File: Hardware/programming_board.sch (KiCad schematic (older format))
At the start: 41 parts, among them J1 Conn_02x03_Odd_Even, J10 Conn_02x03_Odd_Even, J11 Conn_01x05, J12 USB_C_Receptacle_USB2.0, J2 Conn_02x10_Odd_Even, J3 Conn_02x04_Odd_Even, J4 Conn_02x03_Odd_Even, J6 Conn_02x05_Odd_Even, J7 Conn_02x05_Odd_Even, J8 Conn_01x05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

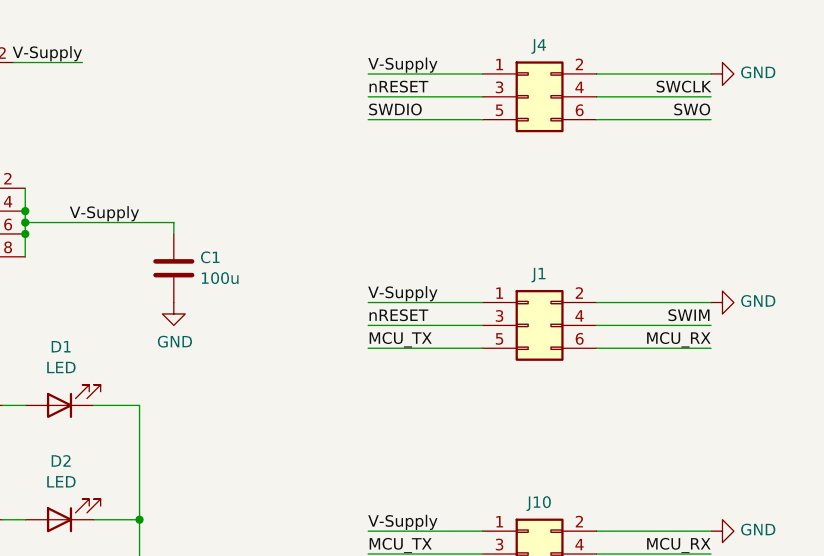
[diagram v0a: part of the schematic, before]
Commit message: add stm8 programming connector; add 3d models
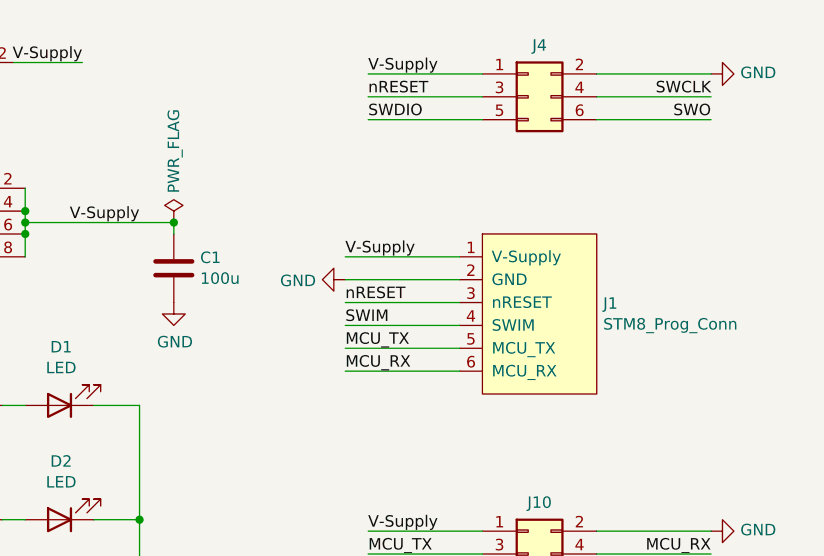
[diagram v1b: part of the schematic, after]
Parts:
- removed J1: Conn_02x03_Odd_Even, custom:IDC-1.27-6P, symbol Connector_Generic:Conn_02x03_Odd_Even
- added J1: STM8_Prog_Conn, local:IDC-1.27-6P, symbol local:STM8_Prog_Conn
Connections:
- net GND: now also J1.2 (GND)
- net MCU_RX: now also J1.6 (MCU_RX)
- net MCU_TX: now also J1.5 (MCU_TX)
- net SWIM: now also J1.4 (SWIM)
- net V-Supply: now also J1.1 (V-Supply)
- net nRESET: now also J1.3 (nRESET)
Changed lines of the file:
@@
 VTref
-$Comp
-L Connector_Generic:Conn_02x03_Odd_Even J4
-U 1 1 615358D8
-P 9700 1150
-F 0 "J4" H 9750 1375 50  0000 C CNN
-F 1 "Conn_02x03_Odd_Even" H 9750 1376 50  0001 C CNN
-F 2 "custom:IDC-1.27-6P" H 9700 1150 50  0001 C CNN
-F 3 "~" H 9700 1150 50  0001 C CNN
-	1    9700 1150
-	1    0    0    -1
-$EndComp
-Wire Wire Line
-	9500 1050 9000 1050
-Wire Wire Line
-	9500 1150 9000 1150
-Wire Wire Line
-	9500 1250 9000 1250
-Wire Wire Line
-	10000 1050 10500 1050
-Wire Wire Line
-	10000 1150 10500 1150
-Wire Wire Line
-	10000 1250 10500 1250
-Text Label 9000 1050 0    50   ~ 0
-V-Supply
-$Comp
-L power:GND #PWR03
-U 1 1 615358E5
-P 10500 1050
-F 0 "#PWR03" H 10500 800 50  0001 C CNN
-F 1 "GND" V 10505 922 50  0000 R CNN
-F 2 "" H 10500 1050 50  0001 C CNN
-F 3 "" H 10500 1050 50  0001 C CNN
-	1    10500 1050
-	0    -1   -1   0
-$EndComp
-Text Label 10500 1150 2    50   ~ 0
-SWCLK
-Text Label 10500 1250 2    50   ~ 0
-SWO
-Text Label 9000 1150 0    50   ~ 0
-nRESET
 $Comp
 L Connector_Generic:Conn_02x03_Odd_Even J10
@@
 	2000 5350 2000 5400
 $Comp
+L Device:C C1
+U 1 1 61B3CD10
+P 8150 1900
+F 0 "C1" H 8265 1946 50  0000 L CNN
+F 1 "100u" H 8265 1855 50  0000 L CNN
+F 2 "Capacitor_SMD:C_1206_3216Metric_Pad1.33x1.80mm_HandSolder" H 8188 1750 50  0001 C CNN
+F 3 "~" H 8150 1900 50  0001 C CNN
+	1    8150 1900
+	1    0    0    -1
+$EndComp
+Wire Wire Line
+	8150 1700 8150 1750
+Wire Wire Line
+	7500 1700 8150 1700
+$Comp
+L power:GND #PWR05
+U 1 1 61B4872C
+P 8150 2050
+F 0 "#PWR05" H 8150 1800 50  0001 C CNN
+F 1 "GND" H 8155 1877 50  0000 C CNN
+F 2 "" H 8150 2050 50  0001 C CNN
+F 3 "" H 8150 2050 50  0001 C CNN
+	1    8150 2050
+	1    0    0    -1
+$EndComp
+$Comp
+L Mechanical:MountingHole_Pad H1
+U 1 1 61B6916F
+P 9050 5500
+F 0 "H1" V 9287 5503 50  0000 C CNN
+F 1 "MountingHole_Pad" V 9196 5503 50  0000 C CNN
+F 2 "MountingHole:MountingHole_3.2mm_M3_Pad_Via" H 9050 5500 50  0001 C CNN
+F 3 "~" H 9050 5500 50  0001 C CNN
+	1    9050 5500
+	0    -1   -1   0
+$EndComp
+$Comp
+L Mechanical:MountingHole_Pad H3
+U 1 1 61B69E0B
+P 9050 6000
+F 0 "H3" V 9287 6003 50  0000 C CNN
+F 1 "MountingHole_Pad" V 9196 6003 50  0000 C CNN
+F 2 "MountingHole:MountingHole_3.2mm_M3_Pad_Via" H 9050 6000 50  0001 C CNN
+F 3 "~" H 9050 6000 50  0001 C CNN
+	1    9050 6000
+	0    -1   -1   0
+$EndComp
+$Comp
+L Mechanical:MountingHole_Pad H2
+U 1 1 61B6A090
+P 9950 5500
+F 0 "H2" V 9904 5650 50  0000 L CNN
+F 1 "MountingHole_Pad" V 9995 5650 50  0000 L CNN
+F 2 "MountingHole:MountingHole_3.2mm_M3_Pad_Via" H 9950 5500 50  0001 C CNN
+F 3 "~" H 9950 5500 50  0001 C CNN
+	1    9950 5500
+	0    1    1    0
+$EndComp
+$Comp
+L Mechanical:MountingHole_Pad H4
+U 1 1 61B6A5E9
+P 9950 6000
+F 0 "H4" V 9904 6150 50  0000 L CNN
+F 1 "MountingHole_Pad" V 9995 6150 50  0000 L CNN
+F 2 "MountingHole:MountingHole_3.2mm_M3_Pad_Via" H 9950 6000 50  0001 C CNN
+F 3 "~" H 9950 6000 50  0001 C CNN
+	1    9950 6000
+	0    1    1    0
+$EndComp
+Wire Wire Line
+	9150 5500 9500 5500
+Wire Wire Line
+	9150 6000 9500 6000
+$Comp
+L power:GND #PWR030
+U 1 1 61B81246
+P 9500 5500
+F 0 "#PWR030" H 9500 5250 50  0001 C CNN
+F 1 "GND" H 9505 5327 50  0000 C CNN
+F 2 "" H 9500 5500 50  0001 C CNN
+F 3 "" H 9500 5500 50  0001 C CNN
+	1    9500 5500
+	1    0    0    -1
+$EndComp
+Connection ~ 9500 5500
+Wire Wire Line
+	9500 5500 9850 5500
+$Comp
+L power:GND #PWR031
+U 1 1 61B81570
+P 9500 6000
+F 0 "#PWR031" H 9500 5750 50  0001 C CNN
+F 1 "GND" H 9505 5827 50  0000 C CNN
+F 2 "" H 9500 6000 50  0001 C CNN
+F 3 "" H 9500 6000 50  0001 C CNN
+	1    9500 6000
+	1    0    0    -1
+$EndComp
+Connection ~ 9500 6000
+Wire Wire Line
+	9500 6000 9850 6000
+Wire Wire Line
+	9400 1850 8900 1850
+Wire Wire Line
+	9400 2050 8900 2050
+Wire Wire Line
+	9400 2250 8900 2250
+Wire Wire Line
+	9400 1950 8900 1950
+Wire Wire Line
+	9400 2150 8900 2150
+Wire Wire Line
+	9400 2350 8900 2350
+Text Label 8900 1850 0    50   ~ 0
+V-Supply
+$Comp
+L power:GND #PWR01
+U 1 1 61CC4E44
+P 8900 1950
+F 0 "#PWR01" H 8900 1700 50  0001 C CNN
+F 1 "GND" V 8905 1822 50  0000 R CNN
+F 2 "" H 8900 1950 50  0001 C CNN
+F 3 "" H 8900 1950 50  0001 C CNN
+	1    8900 1950
+	0    1    1    0
+$EndComp
+Text Label 8900 2050 0    50   ~ 0
+nRESET
+Text Label 8900 2250 0    50   ~ 0
+MCU_TX
+Text Label 8900 2350 0    50   ~ 0
+MCU_RX
+Text Label 8900 2150 0    50   ~ 0
+SWIM
+Text Label 9000 1250 0    50   ~ 0
+SWDIO
+Text Label 9000 1150 0    50   ~ 0
+nRESET
+Text Label 9000 1050 0    50   ~ 0
+V-Supply
+Wire Wire Line
+	9500 1250 9000 1250
+Wire Wire Line
+	9500 1150 9000 1150
+Wire Wire Line
+	9500 1050 9000 1050
+Text Label 10500 1250 2    50   ~ 0
+SWO
+Text Label 10500 1150 2    50   ~ 0
+SWCLK
+$Comp
+L power:GND #PWR03
+U 1 1 615358E5
+P 10500 1050
+F 0 "#PWR03" H 10500 800 50  0001 C CNN
+F 1 "GND" V 10505 922 50  0000 R CNN
+F 2 "" H 10500 1050 50  0001 C CNN
+F 3 "" H 10500 1050 50  0001 C CNN
+	1    10500 1050
+	0    -1   -1   0
+$EndComp
+Wire Wire Line
+	10000 1250 10500 1250
+Wire Wire Line
+	10000 1150 10500 1150
+Wire Wire Line
+	10000 1050 10500 1050
+$Comp
+L local:STM8_Prog_Conn J1
+U 1 1 61519288
+P 10000 1750
+F 0 "J1" H 9972 1446 50  0000 R CNN
+F 1 "STM8_Prog_Conn" H 9972 1355 50  0000 R CNN
+F 2 "local:IDC-1.27-6P" H 10250 1000 50  0001 C CNN
+F 3 "" H 10000 1750 50  0001 C CNN
+	1    10000 1750
+	-1   0    0    -1
+$EndComp
+$Comp
+L Connector_Generic:Conn_02x03_Odd_Even J4
+U 1 1 615358D8
+P 9700 1150
+F 0 "J4" H 9750 1375 50  0000 C CNN
+F 1 "Conn_02x03_Odd_Even" H 9750 1376 50  0001 C CNN
+F 2 "custom:IDC-1.27-6P" H 9700 1150 50  0001 C CNN
+F 3 "~" H 9700 1150 50  0001 C CNN
+	1    9700 1150
+	1    0    0    -1
+$EndComp
+Connection ~ 1350 7250
+$Comp
 L power:PWR_FLAG #FLG02
 U 1 1 61B2F1EC
@@
 	0    1    1    0
 $EndComp
-Connection ~ 1350 7250
-$Comp
-L Device:C C1
-U 1 1 61B3CD10
-P 8150 1900
-F 0 "C1" H 8265 1946 50  0000 L CNN
-F 1 "100u" H 8265 1855 50  0000 L CNN
-F 2 "Capacitor_SMD:C_1206_3216Metric_Pad1.33x1.80mm_HandSolder" H 8188 1750 50  0001 C CNN
-F 3 "~" H 8150 1900 50  0001 C CNN
-	1    8150 1900
-	1    0    0    -1
-$EndComp
-Wire Wire Line
-	8150 1700 8150 1750
-Wire Wire Line
-	7500 1700 8150 1700
-$Comp
-L power:GND #PWR05
-U 1 1 61B4872C
-P 8150 2050
-F 0 "#PWR05" H 8150 1800 50  0001 C CNN
-F 1 "GND" H 8155 1877 50  0000 C CNN
-F 2 "" H 8150 2050 50  0001 C CNN
-F 3 "" H 8150 2050 50  0001 C CNN
-	1    8150 2050
-	1    0    0    -1
-$EndComp
-$Comp
-L Mechanical:MountingHole_Pad H1
-U 1 1 61B6916F
-P 9050 5500
-F 0 "H1" V 9287 5503 50  0000 C CNN
-F 1 "MountingHole_Pad" V 9196 5503 50  0000 C CNN
-F 2 "MountingHole:MountingHole_3.2mm_M3_Pad_Via" H 9050 5500 50  0001 C CNN
-F 3 "~" H 9050 5500 50  0001 C CNN
-	1    9050 5500
-	0    -1   -1   0
-$EndComp
-$Comp
-L Mechanical:MountingHole_Pad H3
-U 1 1 61B69E0B
-P 9050 6000
-F 0 "H3" V 9287 6003 50  0000 C CNN
-F 1 "MountingHole_Pad" V 9196 6003 50  0000 C CNN
-F 2 "MountingHole:MountingHole_3.2mm_M3_Pad_Via" H 9050 6000 50  0001 C CNN
-F 3 "~" H 9050 6000 50  0001 C CNN
-	1    9050 6000
-	0    -1   -1   0
-$EndComp
-$Comp
-L Mechanical:MountingHole_Pad H2
-U 1 1 61B6A090
-P 9950 5500
-F 0 "H2" V 9904 5650 50  0000 L CNN
-F 1 "MountingHole_Pad" V 9995 5650 50  0000 L CNN
-F 2 "MountingHole:MountingHole_3.2mm_M3_Pad_Via" H 9950 5500 50  0001 C CNN
-F 3 "~" H 9950 5500 50  0001 C CNN
-	1    9950 5500
-	0    1    1    0
-$EndComp
-$Comp
-L Mechanical:MountingHole_Pad H4
-U 1 1 61B6A5E9
-P 9950 6000
-F 0 "H4" V 9904 6150 50  0000 L CNN
-F 1 "MountingHole_Pad" V 9995 6150 50  0000 L CNN
-F 2 "MountingHole:MountingHole_3.2mm_M3_Pad_Via" H 9950 6000 50  0001 C CNN
-F 3 "~" H 9950 6000 50  0001 C CNN
-	1    9950 6000
-	0    1    1    0
-$EndComp
-Wire Wire Line
-	9150 5500 9500 5500
-Wire Wire Line
-	9150 6000 9500 6000
-$Comp
-L power:GND #PWR030
-U 1 1 61B81246
-P 9500 5500
-F 0 "#PWR030" H 9500 5250 50  0001 C CNN
-F 1 "GND" H 9505 5327 50  0000 C CNN
-F 2 "" H 9500 5500 50  0001 C CNN
-F 3 "" H 9500 5500 50  0001 C CNN
-	1    9500 5500
-	1    0    0    -1
-$EndComp
-Connection ~ 9500 5500
-Wire Wire Line
-	9500 5500 9850 5500
-$Comp
-L power:GND #PWR031
-U 1 1 61B81570
-P 9500 6000
-F 0 "#PWR031" H 9500 5750 50  0001 C CNN
-F 1 "GND" H 9505 5827 50  0000 C CNN
-F 2 "" H 9500 6000 50  0001 C CNN
-F 3 "" H 9500 6000 50  0001 C CNN
-	1    9500 6000
-	1    0    0    -1
-$EndComp
-Connection ~ 9500 6000
-Wire Wire Line
-	9500 6000 9850 6000
-$Comp
-L Connector_Generic:Conn_02x03_Odd_Even J1
-U 1 1 61CC4E13
-P 9700 2150
-F 0 "J1" H 9750 2375 50  0000 C CNN
-F 1 "Conn_02x03_Odd_Even" H 9750 2376 50  0001 C CNN
-F 2 "custom:IDC-1.27-6P" H 9700 2150 50  0001 C CNN
-F 3 "~" H 9700 2150 50  0001 C CNN
-	1    9700 2150
-	1    0    0    -1
-$EndComp
-Wire Wire Line
-	9500 2050 9000 2050
-Wire Wire Line
-	9500 2150 9000 2150
-Wire Wire Line
-	9500 2250 9000 2250
-Wire Wire Line
-	10000 2050 10500 2050
-Wire Wire Line
-	10000 2150 10500 2150
-Wire Wire Line
-	10000 2250 10500 2250
-Text Label 9000 2050 0    50   ~ 0
-V-Supply
-$Comp
-L power:GND #PWR01
-U 1 1 61CC4E44
-P 10500 2050
-F 0 "#PWR01" H 10500 1800 50  0001 C CNN
-F 1 "GND" V 10505 1922 50  0000 R CNN
-F 2 "" H 10500 2050 50  0001 C CNN
-F 3 "" H 10500 2050 50  0001 C CNN
-	1    10500 2050
-	0    -1   -1   0
-$EndComp
-Text Label 9000 2150 0    50   ~ 0
-nRESET
-Text Label 9000 2250 0    50   ~ 0
-MCU_TX
-Text Label 10500 2250 2    50   ~ 0
-MCU_RX
-Text Label 10500 2150 2    50   ~ 0
-SWIM
-Text Label 9000 1250 0    50   ~ 0
-SWDIO
+$Comp
+L power:PWR_FLAG #FLG0101
+U 1 1 615A6DEA
+P 8150 1700
+F 0 "#FLG0101" H 8150 1775 50  0001 C CNN
+F 1 "PWR_FLAG" V 8150 1828 50  0000 L CNN
+F 2 "" H 8150 1700 50  0001 C CNN
+F 3 "~" H 8150 1700 50  0001 C CNN
+	1    8150 1700
+	1    0    0    -1
+$EndComp
+Connection ~ 8150 1700
 $EndSCHEMATC
